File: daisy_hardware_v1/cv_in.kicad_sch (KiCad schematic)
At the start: 5 parts, among them J18 PJ398SM-12

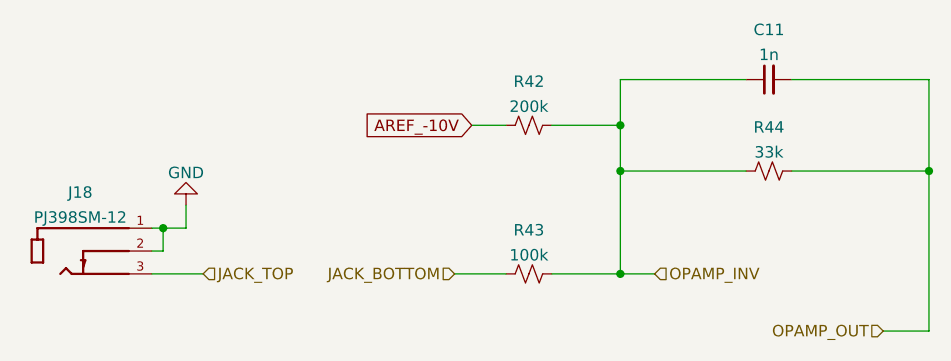
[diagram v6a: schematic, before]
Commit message: SPDT footprint
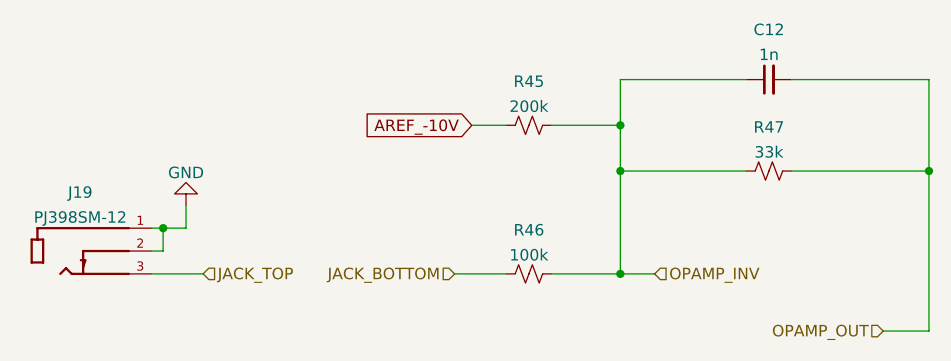
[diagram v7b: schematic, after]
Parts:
- renumbered C11 to C12, J18 to J19, R42 to R45, R43 to R46, R44 to R47
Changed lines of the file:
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@@
   (symbol (lib_id "Device:R_Small_US") (at 96.52 63.5 90)
     (in_bom yes) (on_board yes) (fields_autoplaced)
-    (property "Reference" "R42" (id 0) (at 96.52 58.6445 90))
+    (property "Reference" "R45" (id 0) (at 96.52 58.6445 90))
     (property "Value" "200k" (id 1) (at 96.52 61.4196 90))
     (property "Footprint" "Resistor_SMD:R_0603_1608Metric" (id 2) (at 96.52 63.5 0)
@@
   (symbol (lib_id "PJ398SM-12:PJ398SM-12") (at 46.99 74.93 0)
     (in_bom yes) (on_board yes) (fields_autoplaced)
-    (property "Reference" "J18" (id 0) (at 46.6725 70.9635 0))
+    (property "Reference" "J19" (id 0) (at 46.6725 70.9635 0))
     (property "Value" "PJ398SM-12" (id 1) (at 46.6725 73.7386 0))
     (property "Footprint" "lowstepper_internal_footprint_lib:THONK_PJ398SM-12" (id 2) (at 46.99 74.93 0)
@@
   (symbol (lib_id "Device:C_Small") (at 123.19 58.42 90)
     (in_bom yes) (on_board yes) (fields_autoplaced)
-    (property "Reference" "C11" (id 0) (at 123.1963 52.8914 90))
+    (property "Reference" "C12" (id 0) (at 123.1963 52.8914 90))
     (property "Value" "1n" (id 1) (at 123.1963 55.6665 90))
     (property "Footprint" "Capacitor_SMD:C_0603_1608Metric" (id 2) (at 123.19 58.42 0)
@@
   (symbol (lib_id "Device:R_Small_US") (at 96.52 80.01 90)
     (in_bom yes) (on_board yes) (fields_autoplaced)
-    (property "Reference" "R43" (id 0) (at 96.52 75.1545 90))
+    (property "Reference" "R46" (id 0) (at 96.52 75.1545 90))
     (property "Value" "100k" (id 1) (at 96.52 77.9296 90))
     (property "Footprint" "Resistor_SMD:R_0603_1608Metric" (id 2) (at 96.52 80.01 0)
@@
   (symbol (lib_id "Device:R_Small_US") (at 123.19 68.58 90)
     (in_bom yes) (on_board yes) (fields_autoplaced)
-    (property "Reference" "R44" (id 0) (at 123.19 63.7245 90))
+    (property "Reference" "R47" (id 0) (at 123.19 63.7245 90))
     (property "Value" "33k" (id 1) (at 123.19 66.4996 90))
     (property "Footprint" "Resistor_SMD:R_0603_1608Metric" (id 2) (at 123.19 68.58 0)

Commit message: board connectors expanded
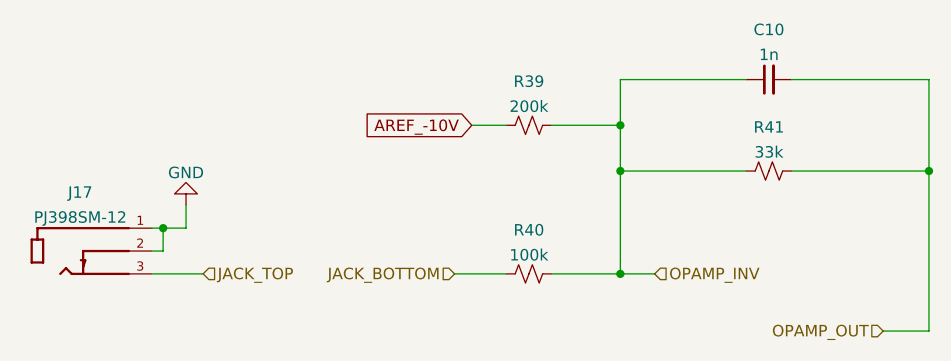
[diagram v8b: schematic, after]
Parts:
- renumbered C12 to C10, J19 to J17, R45 to R39, R46 to R40, R47 to R41
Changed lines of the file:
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@@
   (symbol (lib_id "Device:R_Small_US") (at 96.52 63.5 90)
     (in_bom yes) (on_board yes) (fields_autoplaced)
-    (property "Reference" "R45" (id 0) (at 96.52 58.6445 90))
+    (property "Reference" "R39" (id 0) (at 96.52 58.6445 90))
     (property "Value" "200k" (id 1) (at 96.52 61.4196 90))
     (property "Footprint" "Resistor_SMD:R_0603_1608Metric" (id 2) (at 96.52 63.5 0)
@@
   (symbol (lib_id "PJ398SM-12:PJ398SM-12") (at 46.99 74.93 0)
     (in_bom yes) (on_board yes) (fields_autoplaced)
-    (property "Reference" "J19" (id 0) (at 46.6725 70.9635 0))
+    (property "Reference" "J17" (id 0) (at 46.6725 70.9635 0))
     (property "Value" "PJ398SM-12" (id 1) (at 46.6725 73.7386 0))
     (property "Footprint" "lowstepper_internal_footprint_lib:THONK_PJ398SM-12" (id 2) (at 46.99 74.93 0)
@@
   (symbol (lib_id "Device:C_Small") (at 123.19 58.42 90)
     (in_bom yes) (on_board yes) (fields_autoplaced)
-    (property "Reference" "C12" (id 0) (at 123.1963 52.8914 90))
+    (property "Reference" "C10" (id 0) (at 123.1963 52.8914 90))
     (property "Value" "1n" (id 1) (at 123.1963 55.6665 90))
     (property "Footprint" "Capacitor_SMD:C_0603_1608Metric" (id 2) (at 123.19 58.42 0)
@@
   (symbol (lib_id "power:GND") (at 58.42 72.39 180)
     (in_bom yes) (on_board yes)
-    (property "Reference" "#PWR0189" (id 0) (at 58.42 66.04 0)
+    (property "Reference" "#PWR0165" (id 0) (at 58.42 66.04 0)
       (effects (font (size 1.27 1.27)) hide)
     )
@@
   (symbol (lib_id "Device:R_Small_US") (at 96.52 80.01 90)
     (in_bom yes) (on_board yes) (fields_autoplaced)
-    (property "Reference" "R46" (id 0) (at 96.52 75.1545 90))
+    (property "Reference" "R40" (id 0) (at 96.52 75.1545 90))
     (property "Value" "100k" (id 1) (at 96.52 77.9296 90))
     (property "Footprint" "Resistor_SMD:R_0603_1608Metric" (id 2) (at 96.52 80.01 0)
@@
   (symbol (lib_id "Device:R_Small_US") (at 123.19 68.58 90)
     (in_bom yes) (on_board yes) (fields_autoplaced)
-    (property "Reference" "R47" (id 0) (at 123.19 63.7245 90))
+    (property "Reference" "R41" (id 0) (at 123.19 63.7245 90))
     (property "Value" "33k" (id 1) (at 123.19 66.4996 90))
     (property "Footprint" "Resistor_SMD:R_0603_1608Metric" (id 2) (at 123.19 68.58 0)
